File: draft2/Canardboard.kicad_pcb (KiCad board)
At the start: 4 copper layers, 159.3 x 124.4 mm, 111 parts, among them IC1 SIC437DED-T1-GE3, J1 RBUS, J2 USB_C_Receptacle_USB2.0, J3 Micro_SD_Card_Det, J4 Conn_01x02_Male, J5 Conn_01x03_Male, J6 Conn_01x03_Male, J7 Conn_01x03_Male, Q1 SI4143DY-T1-GE3, Q2 SI4143DY-T1-GE3, U1 ESP32-S3, U10 LTC4412xS6, U2 SN65HVD230, U3 LM66200DRLR, U5 MAX77827AEFD+T, U6 SC4215, U7 ICM-20608-G, U8 MMC5983MA, U9 LTC4412xS6, Y1 40MHz±10ppm

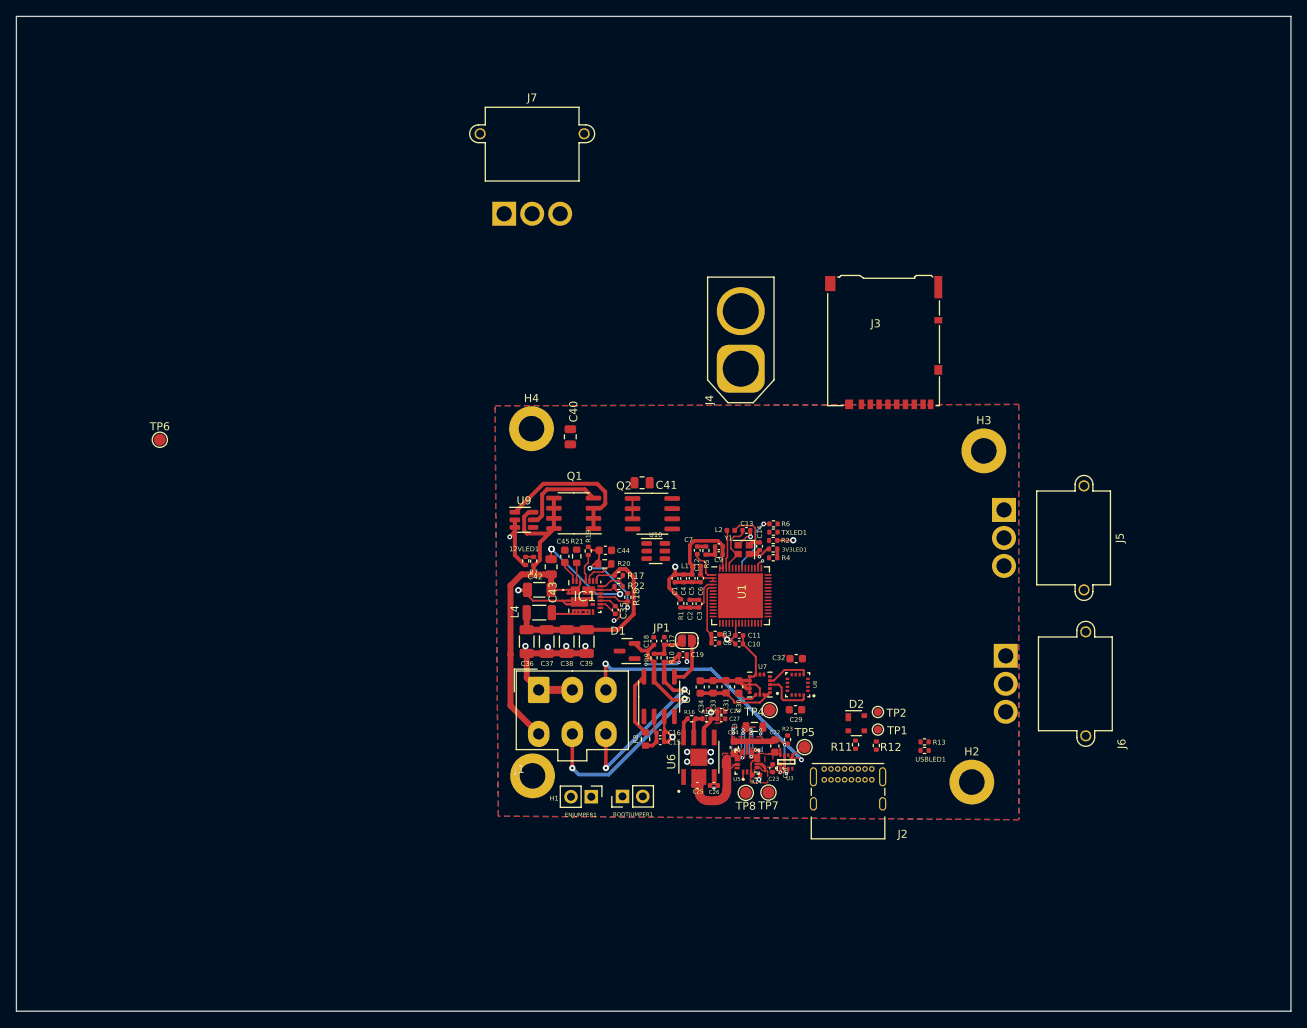
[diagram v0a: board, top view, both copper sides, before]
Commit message: 11/02/23
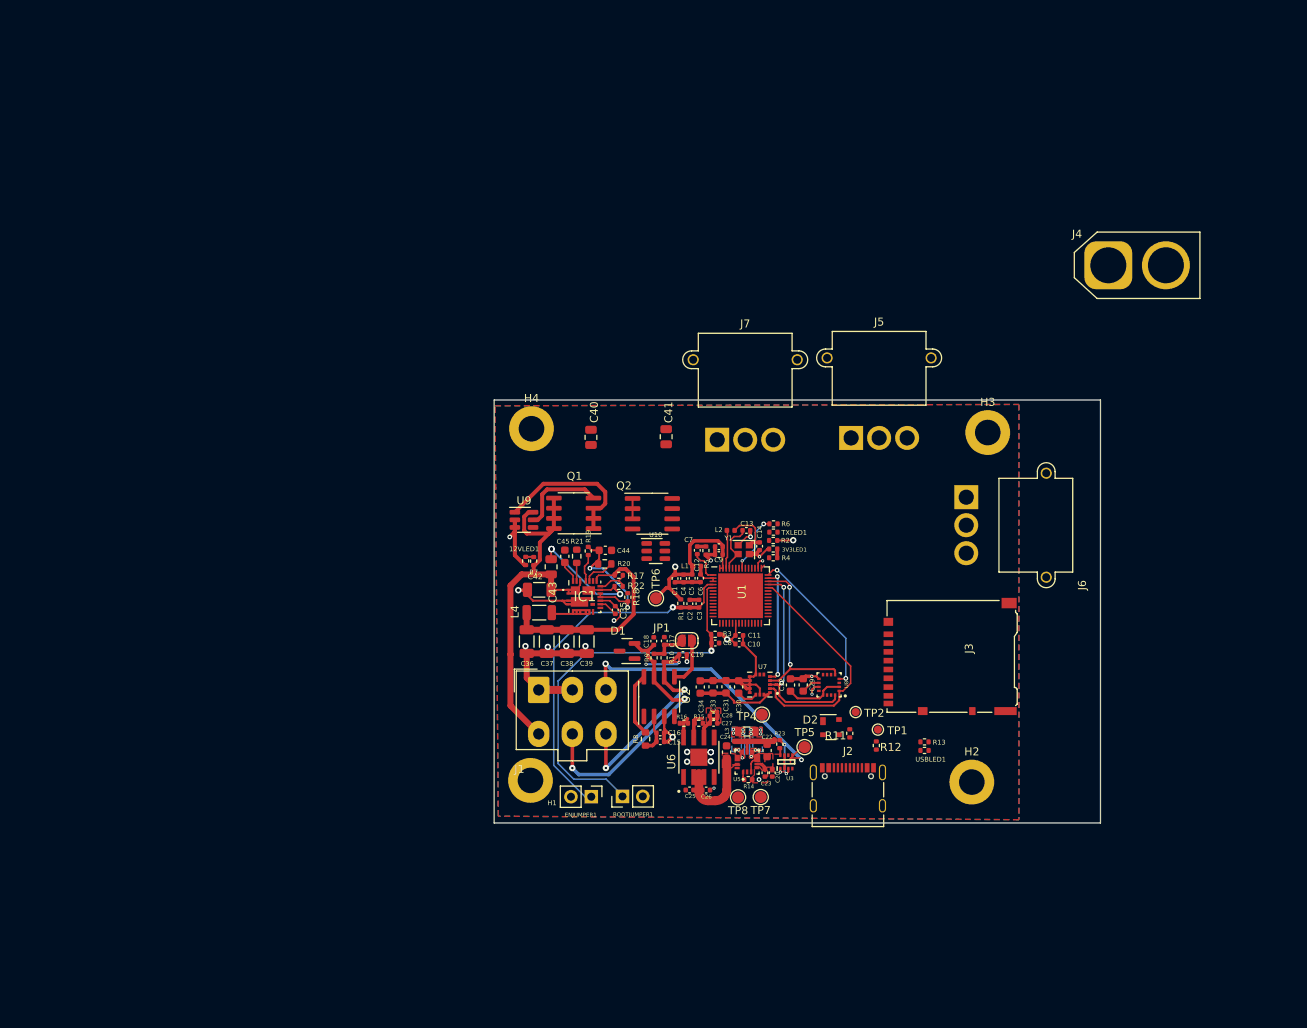
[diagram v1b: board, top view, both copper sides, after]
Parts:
- J2: footprint Connector_USB:USB_C_Receptacle_GCT_USB4085 -> Connector_USB:USB_C_Receptacle_Palconn_UTC16-G
- moved TP6 65.1 mm to (116.1, 98.2)
- moved J4 47.7 mm to (172.7, 56.6), turned to 0 degrees
- moved J3 40.1 mm to (152.9, 105.5), turned to 90 degrees
- moved J7 38.8 mm to (123.8, 78.4)
- moved J5 21.1 mm to (140.5, 78.2), turned to 0 degrees
- moved J6 20.4 mm to (154.9, 85.6)
- moved C41 6.49 mm to (117.4, 78.0), turned to -90 degrees
- moved U8 3.93 mm to (137.8, 109.0)
- moved J2 3.79 mm to (140.1, 121.9)
- moved C32 3.37 mm to (132.9, 109.1), turned to 90 degrees
- moved C29 3.25 mm to (134.5, 109.0), turned to 90 degrees
- moved D2 3.21 mm to (138.0, 114.3)
- moved TP2 2.78 mm to (141.1, 112.4)
- moved C40 2.58 mm to (108.0, 78.1)
- moved H3 2.34 mm to (157.6, 77.5)
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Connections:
- L4 pad 1: /comps/SW -> /SERVO_PWR
- L4 pad 2: /SERVO_PWR -> /comps/SW
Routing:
- net GND: track 88.7 -> 137.5 mm, vias 18 -> 21
- net /BOOT: track 7.75 -> 49.6 mm, vias 0 -> 1
- net /CHIP_PU: track 6.28 -> 45.2 mm, vias 0 -> 1
- net RBUS_uC_V: track 37.1 -> 0.00 mm
- net /SPI_CLK: track 0.00 -> 29.8 mm
- net /MAG_CS: track 0.00 -> 19.4 mm, vias 0 -> 2
- net /SPI_MOSI: track 6.48 -> 25.5 mm, vias 0 -> 2
- net /SPI_MISO: track 5.32 -> 22.8 mm, vias 0 -> 2
- net /IMU_CS: track 0.00 -> 14.6 mm, vias 0 -> 2
- net +3V3: track 40.2 -> 49.7 mm, vias 5 -> 4
- net VBUS: track 5.27 -> 0.00 mm
- net Net-(C29-Pad1): track 0.02 -> 2.39 mm
- net /SD_CS: track 0.00 -> 0.53 mm
- net Net-(R6-Pad2): track 7.41 -> 7.42 mm, vias 1 -> 2
- net /Power/LX2: vias 5 -> 4
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- added copper zone on In2.Cu, net +3V3
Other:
- board size 159.3 x 124.4 mm -> 75.8 x 52.9 mm

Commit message: changes
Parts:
- moved J4 67.5 mm to (109.1, 79.2)
- moved J6 35.6 mm to (147.3, 120.4), turned to 180 degrees
- moved J3 24.8 mm to (147.0, 81.4), turned to 180 degrees
- moved J5 18.7 mm to (147.7, 95.4), turned to -90 degrees
- moved J2 16.1 mm to (153.3, 112.8), turned to 90 degrees
- moved C40 10.1 mm to (99.1, 82.8)
- moved J7 8.25 mm to (127.2, 85.9)
- moved C41 8.25 mm to (113.0, 85.0), turned to 0 degrees
- moved R11 8.20 mm to (148.5, 114.2), turned to 180 degrees
- moved D2 7.92 mm to (145.8, 113.0)
- moved R12 7.47 mm to (148.7, 111.1), turned to 0 degrees
- moved TP2 5.73 mm to (146.4, 110.3)
- moved U10 5.27 mm to (112.8, 88.2)
- moved USBLED1 3.74 mm to (146.5, 115.3)
- moved Q2 2.97 mm to (118.6, 87.2), turned to 180 degrees
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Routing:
- net /SERVO_PWR: track 27.5 -> 97.1 mm
- net GND: track 137.5 -> 178.2 mm, vias 21 -> 31
- net RBUS_uC_V: track 0.00 -> 33.8 mm
- net /SERVO_SGNL2: track 0.00 -> 29.7 mm, vias 0 -> 2
- net +3V3: track 49.7 -> 75.4 mm, vias 4 -> 7
- net Net-(J4-Pin_1): track 2.92 -> 26.4 mm
- net /SPI_CLK: track 29.8 -> 52.7 mm, vias 0 -> 4
- net /SPI_MISO: track 22.8 -> 45.2 mm, vias 2 -> 5
- net /SERVO_SGNL1: track 0.00 -> 20.3 mm, vias 0 -> 2
- net VBUS: track 0.00 -> 20.0 mm
- net /SPI_MOSI: track 25.5 -> 43.6 mm, vias 2 -> 4
- net /SD_CS: track 0.53 -> 18.5 mm, vias 0 -> 2
- net /SERVO_SGNL3: track 1.34 -> 15.6 mm, vias 1 -> 3
- net Net-(Q2-G): track 0.00 -> 13.4 mm
- net +12V: track 49.5 -> 62.3 mm, vias 0 -> 2
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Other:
- board size 75.8 x 52.9 mm -> 65.7 x 52.9 mm
